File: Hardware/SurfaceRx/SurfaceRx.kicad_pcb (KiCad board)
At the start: 2 copper layers, 24.3 x 38.1 mm, 29 parts, among them IC1 SC189ZSKTRT, J1 Conn_01x03, J2 Conn_01x03, J3 Conn_01x03, J4 Conn_01x03, J5 Conn_01x03, J6 Conn_01x03, J7 Conn_01x05, J8 Conn_01x03, P1 VDD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

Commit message: Reverted debug header to pads. Added status LED
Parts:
- added C12: 100nF, Capacitor_SMD:C_0603_1608Metric, F.Cu at (69.1, 61.0)
- added D1: LED, LED_SMD:LED_0603_1608Metric, F.Cu at (47.0, 40.6)
- added R3: 220, Resistor_SMD:R_0603_1608Metric, F.Cu at (51.0, 40.6)
- added U2: CAT24C512, Package_SO:TSSOP-8_4.4x3mm_P0.65mm, F.Cu at (69.1, 63.5)
- C3: moved to B.Cu
- moved C3 61.0 mm to (77.3, 73.4), turned to -90 degrees
- moved C4 58.3 mm to (77.3, 74.9), turned to -90 degrees
- moved C5 52.2 mm to (77.3, 71.9), turned to 90 degrees
- moved C1 46.2 mm to (55.0, 74.9), turned to -90 degrees
- moved C2 37.6 mm to (55.0, 71.9), turned to 90 degrees
- moved P5 29.0 mm to (59.7, 57.1)
- moved P2 26.9 mm to (59.7, 49.5)
- moved P4 25.9 mm to (59.7, 54.6)
- moved P3 25.9 mm to (59.7, 52.1)
- moved P1 22.5 mm to (59.7, 47.0)
- moved J6 7.62 mm to (74.2, 64.8)
- moved C7 3.21 mm to (61.3, 62.2)
- moved L1 3.21 mm to (57.6, 65.7)
- moved C6 3.21 mm to (62.3, 67.3)
- moved IC1 3.21 mm to (61.5, 64.8)
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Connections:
- net CE renamed NRF24_CE
- net CSN renamed NRF24_CSN
- net ESC_SCL renamed I2C_SCL
- net ESC_SDA renamed I2C_SDA
- net MISO renamed SPI_MISO
- net MOSI renamed SPI_MOSI
- net SCK renamed SPI_SCK
- U1 pad 23: unconnected-(U1-Pad23) -> LED_STATUS
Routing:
- net VCC: track 28.0 -> 22.7 mm

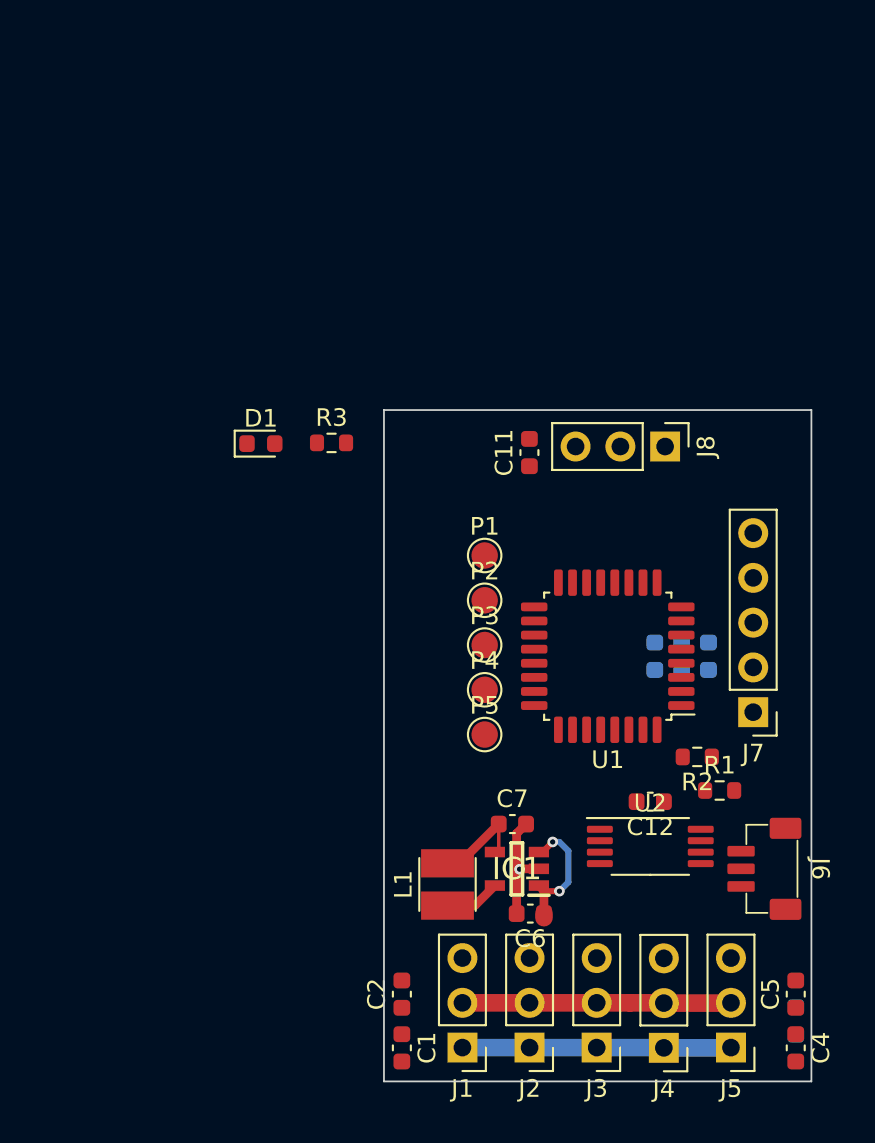
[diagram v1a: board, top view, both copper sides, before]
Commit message: Modified PCB layout
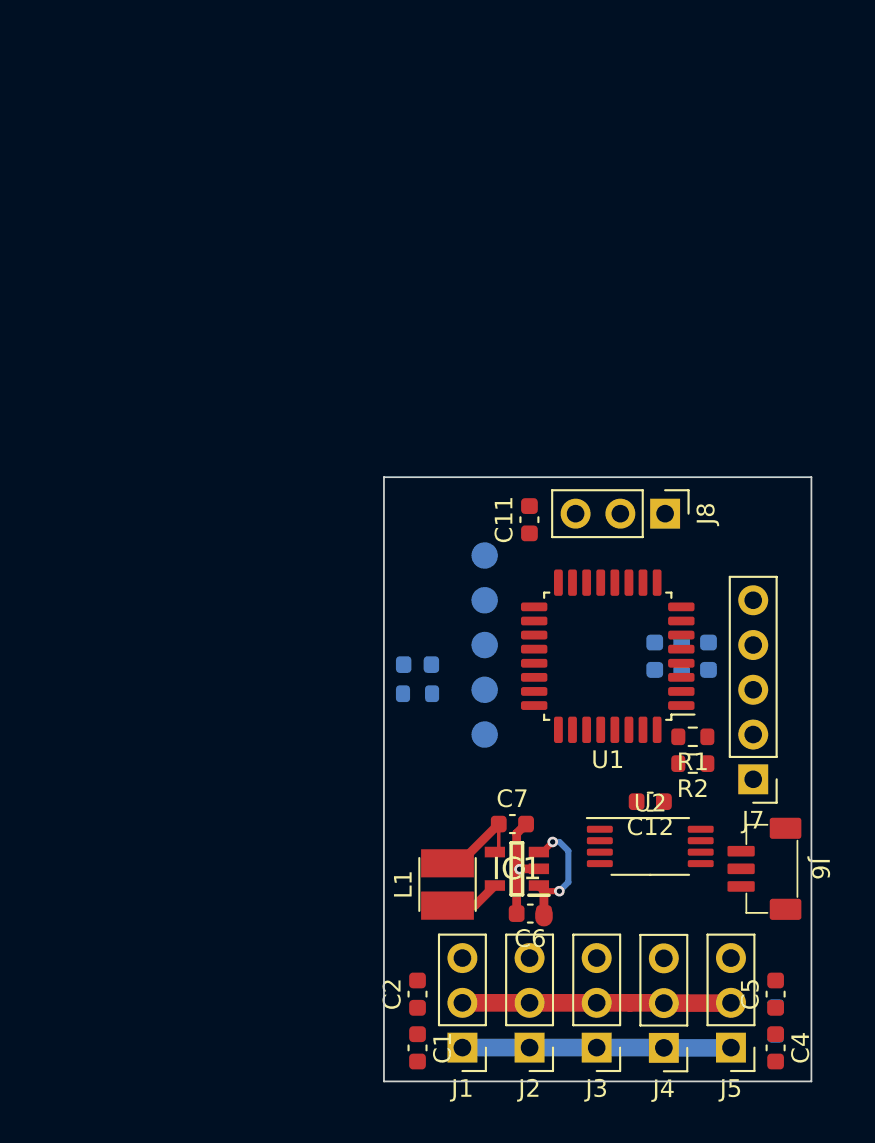
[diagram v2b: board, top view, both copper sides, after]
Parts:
- D1, P1, P2, P3, P4, P5, R3: moved to B.Cu
- moved D1 15.4 mm to (55.9, 53.2), turned to 180 degrees
- moved R3 15.0 mm to (55.9, 54.8)
- moved J8 3.81 mm to (69.9, 44.6)
- moved C11 3.81 mm to (62.2, 45.0)
- moved J7 3.81 mm to (74.9, 59.7)
- moved R1 3.41 mm to (71.5, 57.3), turned to 180 degrees
- moved C3 1.14 mm to (76.2, 73.4)
- moved C4 1.14 mm to (76.2, 74.9)
- moved C5 1.14 mm to (76.2, 71.9)
- moved C1 0.89 mm to (55.9, 74.9)
- moved C2 0.89 mm to (55.9, 71.9)
- moved R2 0.46 mm to (71.5, 58.8)
- turned P1 to 180 degrees
- turned P2 to 180 degrees
- turned P3 to 180 degrees
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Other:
- board size 24.3 x 38.1 mm -> 24.3 x 34.3 mm

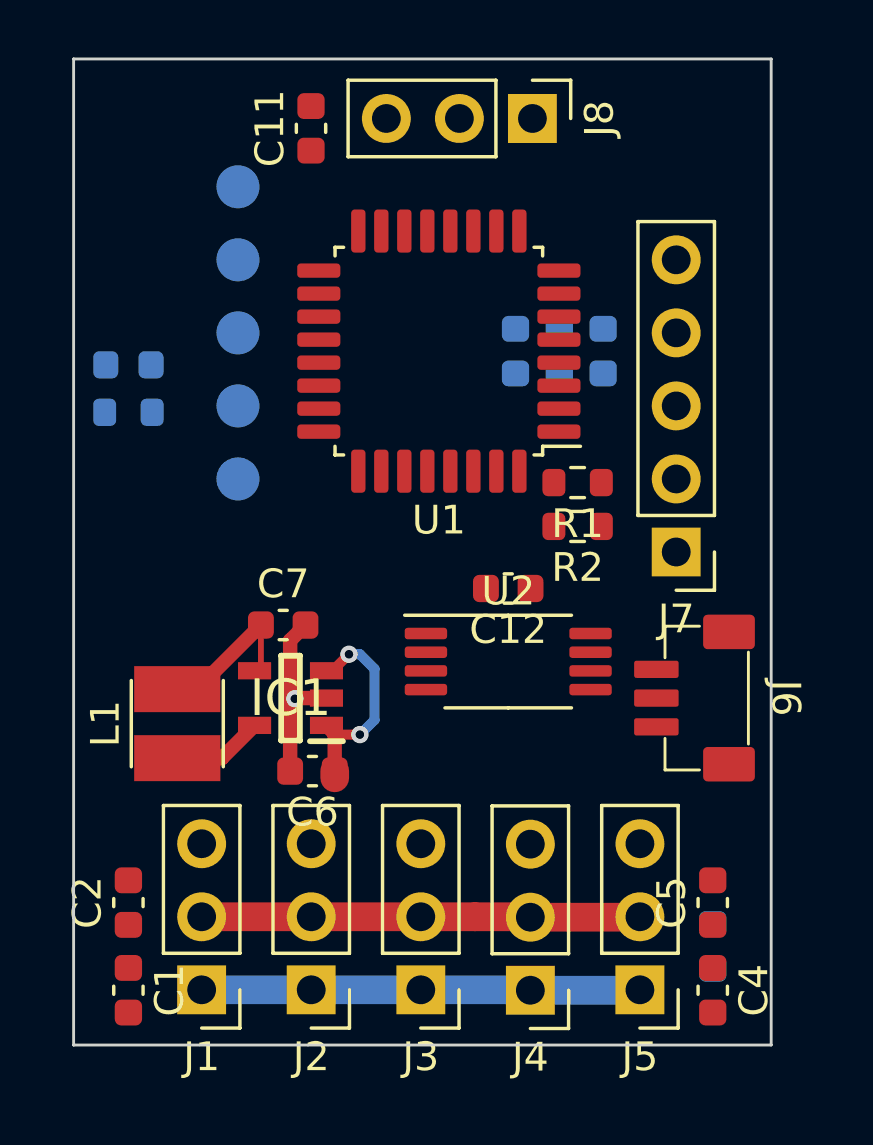
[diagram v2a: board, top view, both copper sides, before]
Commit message: Added ground plane, some traces routed
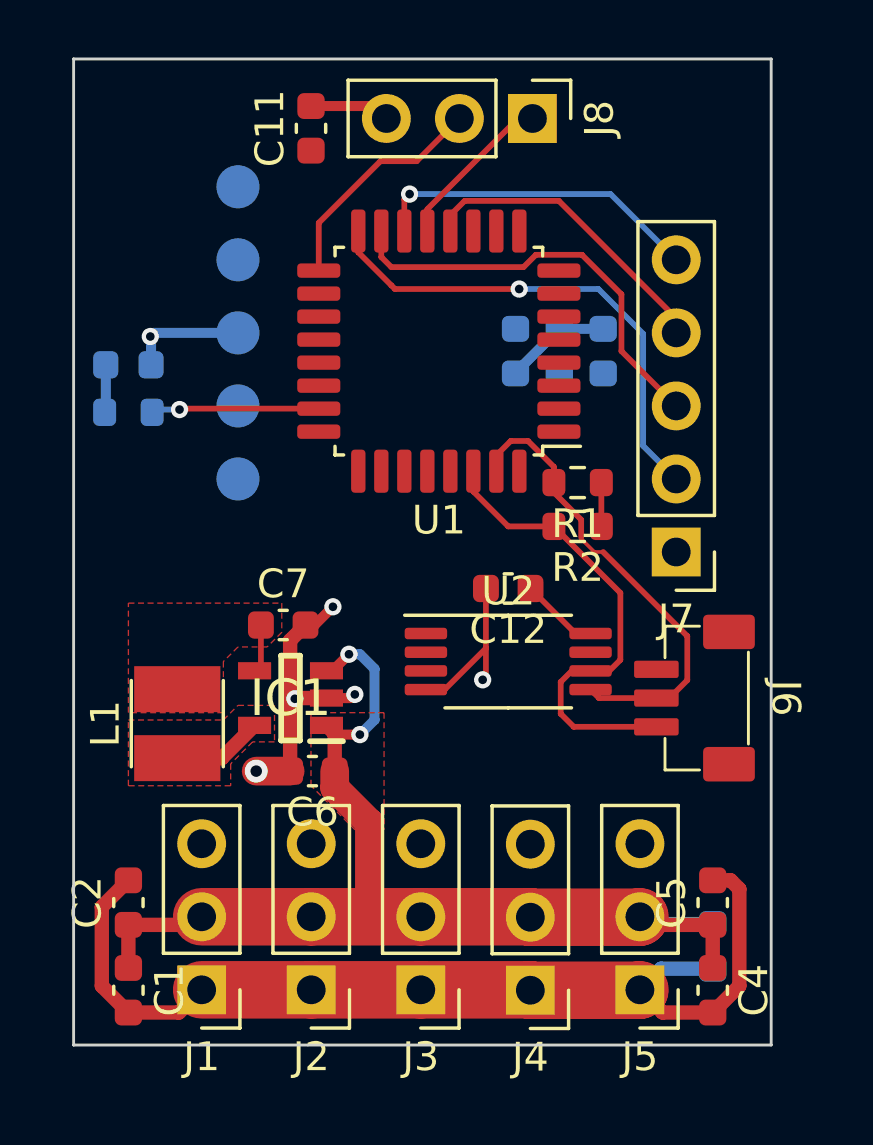
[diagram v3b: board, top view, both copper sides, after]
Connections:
- P1 pad 1: +3.3V -> +3V3
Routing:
- net GND: track 21.9 -> 69.9 mm, vias 1 -> 6
- net NRF24_CE: track 0.00 -> 17.3 mm, vias 0 -> 1
- net I2C_SCL: track 0.00 -> 16.6 mm
- net I2C_SDA: track 0.00 -> 16.4 mm
- net VCC: track 22.7 -> 38.0 mm
- net NRF24_CSN: track 0.00 -> 14.8 mm
- net SPI_MOSI: track 0.00 -> 11.6 mm, vias 0 -> 1
- net SPI_SCK: track 0.00 -> 10.8 mm
- net IRQ: track 0.00 -> 8.05 mm
- net LED_STATUS: track 0.00 -> 5.85 mm, vias 0 -> 1
- net SPI_MISO: track 0.00 -> 5.72 mm
- net Net-(D1-Pad2): track 0.00 -> 1.67 mm
- added copper zone on F.Cu, net +3V3
- added copper zone on In1.Cu, net GND
- added copper zone on F.Cu, net Net-(IC1-Pad5)
- added copper zone on F.Cu, net VCC
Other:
- copper layers 2 -> 4

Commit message: Routed all traces
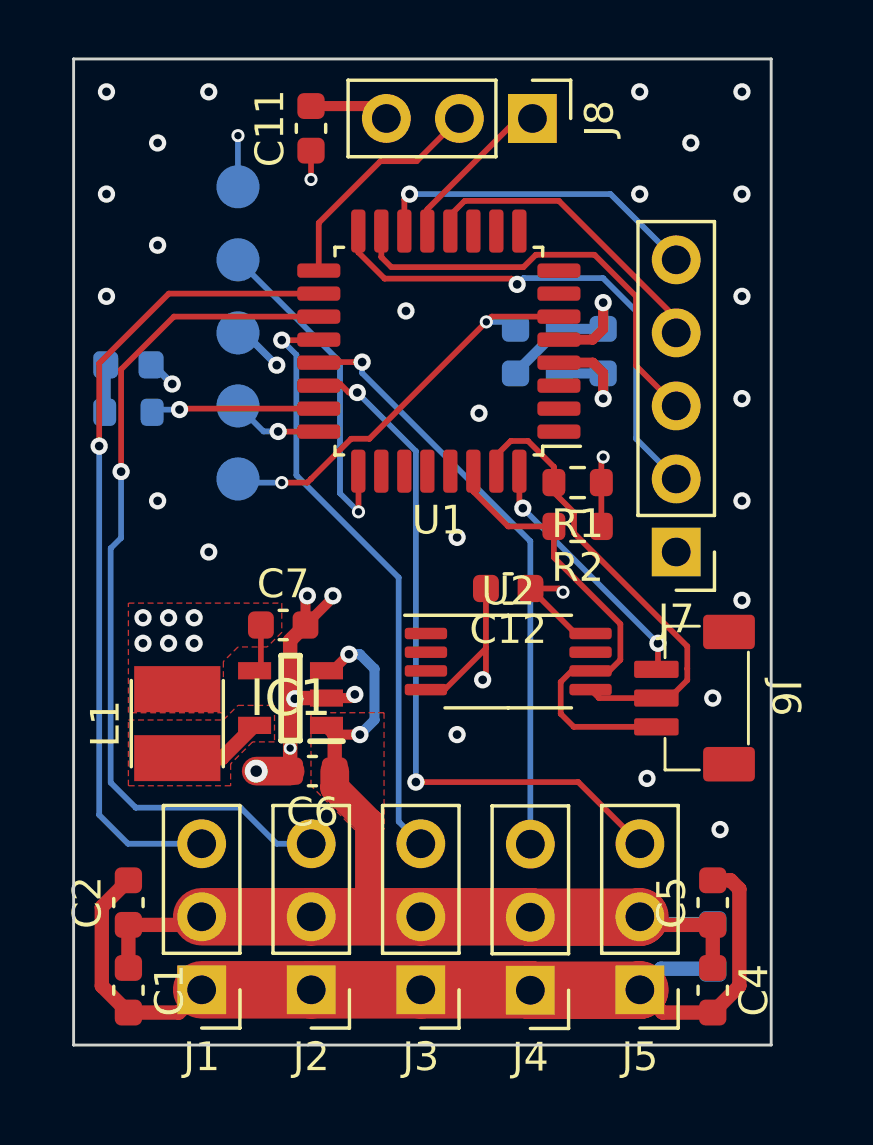
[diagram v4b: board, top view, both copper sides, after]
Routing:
- net STR: track 0.00 -> 30.0 mm, vias 0 -> 1
- net THR: track 0.00 -> 28.3 mm, vias 0 -> 1
- net AUX3: track 0.00 -> 24.6 mm, vias 0 -> 2
- net AUX1: track 0.00 -> 20.8 mm, vias 0 -> 1
- net AUX2: track 0.00 -> 20.7 mm, vias 0 -> 1
- net NRST: track 0.00 -> 14.7 mm, vias 0 -> 2
- net SWCLK: track 0.00 -> 11.9 mm, vias 0 -> 1
- net +3V3: track 5.94 -> 15.8 mm, vias 0 -> 11
- net ESC_INT: track 0.00 -> 8.91 mm, vias 0 -> 2
- net GND: track 69.9 -> 73.4 mm, vias 6 -> 34
- net SWDIO: track 0.00 -> 3.18 mm, vias 0 -> 1
- added copper zone on In2.Cu, net +3V3
- added copper zone on B.Cu, net GND
- added copper zone on F.Cu, net GND

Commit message: Hid reference designators from silkscreen. Added silkscreen labels for servo and ESC outputs.
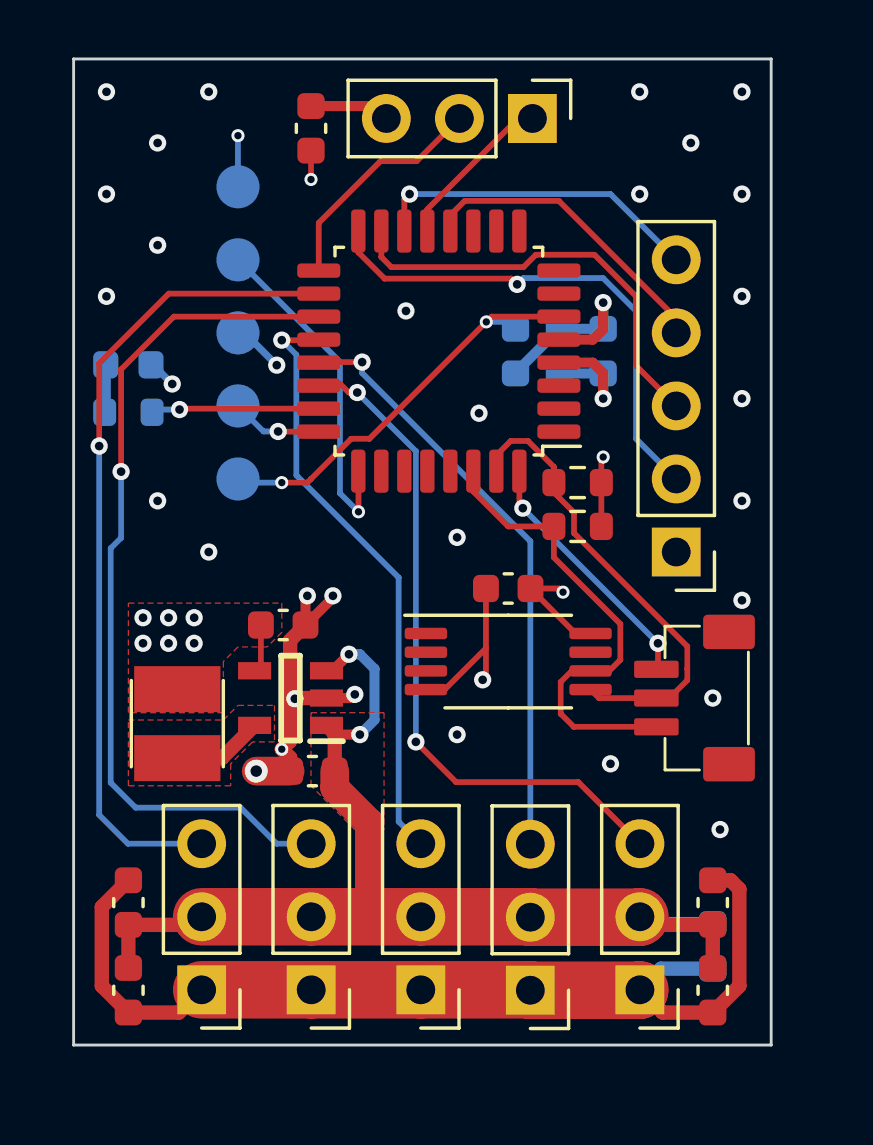
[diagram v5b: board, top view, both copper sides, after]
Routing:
- net AUX3: track 24.6 -> 23.7 mm
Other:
- board text added: "1"
- board text added: "A1"
- board text added: "A2"
- board text added: "A3"
- board text added: "STR"
- board text added: "THR"

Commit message: Added reference designators on PCB for SMD components only. Changed designator from 'IC1' to 'U3'.
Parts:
- renumbered IC1 to U3
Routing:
- net GND: track 73.7 -> 74.2 mm

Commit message: Exported paste layer.
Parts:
- moved R1 0.51 mm to (71.5, 57.8)
- moved R2 0.51 mm to (71.5, 59.3)
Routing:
- net GND: track 74.2 -> 70.5 mm, vias 34 -> 11
- net ESC_INT: track 8.91 -> 11.8 mm
- net I2C_SDA: track 16.2 -> 15.5 mm
- removed copper zone on B.Cu, net GND
